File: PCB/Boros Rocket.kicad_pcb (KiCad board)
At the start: 6 copper layers, 100.6 x 100.6 mm, 44 parts, among them J1 B2B-XH-A, J2 TYPE-C-31-M-12, J3 Conn_01x02_Pin, Q1 MMBT3904, U1 BMP390, U2 IAM-20381, U3 ICM-42688-P, U4 MCP73831T-2DCI_MC, U5 RP2040, U6 USBLC6-2SC6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

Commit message: Refactor code structure for improved readability and maintainability
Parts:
- removed C10, C9: 100 nF, Capacitor_SMD:C_0603_1608Metric
- removed C11, C19: 1µF, Capacitor_SMD:C_0603_1608Metric
- removed C17, C18: 22pF, Capacitor_SMD:C_0603_1608Metric
- removed C20, C7, C8: 100nF, Capacitor_SMD:C_0603_1608Metric
- removed J3: Conn_01x02_Pin, Connector_PinHeader_2.54mm:PinHeader_1x02_P2.54mm_Vertical
- removed R5: 22Ω, Resistor_SMD:R_0603_1608Metric
- removed R7: 10k, Resistor_SMD:R_0603_1608Metric
- removed U5: RP2040, OPL:QFN40P700X700X90-57N
- removed U8: W25Q32JVSSIQ, OPL:SOIC127P790X216-8N
- removed Y1: 12MHz, Crystal:Crystal_SMD_3225-4Pin_3.2x2.5mm
- added J4: Conn_02x04_Counter_Clockwise, Connector_PinHeader_2.54mm:PinHeader_2x04_P2.54mm_Vertical, F.Cu at (136.8, 100.7)
- J2: value TYPE-C-31-M-12 -> 1981568-1; footprint OPL:HRO_TYPE-C-31-M-12 -> OPL:TE_1981568-1
- R1, R2: value 5.1 kΩ -> 100k
- R4: value 22Ω -> 10k
- U2: value IAM-20381 -> STM32G071K8TxN; footprint OPL:PQFN50P300X300X80-16N -> Package_QFP:LQFP-32_7x7mm_P0.8mm
- moved C5 83.1 mm to (154.4, 141.4), turned to 90 degrees
- moved J2 66.0 mm to (147.8, 148.3), turned to 0 degrees
- moved U1 63.9 mm to (130.1, 94.8), turned to 90 degrees
- moved U6 62.4 mm to (144.9, 137.7)
- moved R1 59.0 mm to (151.1, 137.6), turned to 0 degrees
- moved J1 59.0 mm to (194.4, 107.2), turned to -90 degrees
- moved R2 52.1 mm to (169.7, 71.6), turned to 0 degrees
- moved VR1 48.4 mm to (180.8, 109.7), turned to 0 degrees
- moved C12 47.6 mm to (120.9, 100.7), turned to 0 degrees
- moved C13 46.5 mm to (138.0, 90.0), turned to 0 degrees
- moved C15 46.2 mm to (183.2, 103.4), turned to 0 degrees
- moved U3 45.0 mm to (184.6, 83.0), turned to 90 degrees
- moved LS1 41.2 mm to (136.1, 60.2)
- moved C3 38.4 mm to (170.6, 110.2)
- moved C4 35.5 mm to (174.2, 100.5), turned to 90 degrees
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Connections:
- C5 pad 1: 3V3 -> GND
- C5 pad 2: GND -> USB_VBUS_SENSE
- C6 pad 1: 3V3 -> NRST
- R1 pad 1: GND -> USB_VBUS_SENSE
- R1 pad 2: Net-(J2-CC1) -> USB_VBUS
- R2 pad 1: GND -> USB_VBUS_SENSE
- R2 pad 2: Net-(J2-CC2) -> GND
- R4 pad 1: USB_DP -> 3V3
- R4 pad 2: Net-(U5-USB_DP) -> NRST
- U1 pad INT: BARO_INT -> unconnected-(U1-PadINT)
- U2 pad 1: 3V3 -> BUZZER_EN
- U2 pad 10: unconnected-(U2-RESV9_1215-Pad10)_1 -> UART_RX
- U2 pad 11: unconnected-(U2-RESV9_1215-Pad10) -> FLASH_CS
- U2 pad 12: unconnected-(U2-RESV9_1215-Pad10)_3 -> SPI_SCK
- U2 pad 13: GND -> SPI_MISO
- U2 pad 14: Net-(U2-REGOUT) -> SPI_MOSI
- U2 pad 15: unconnected-(U2-RESV9_1215-Pad10)_2 -> IMU_CS
- U2 pad 16: 3V3 -> BARO_CS
- U2 pad 2: SPI_SCK -> unconnected-(U2-PC14-Pad2)
- U2 pad 3: SPI_MOSI -> CHG_STAT
- U2 pad 4: SPI_MISO -> 3V3
- U2 pad 5: GYRO_CS -> GND
- U2 pad 6: IMU_INT -> NRST
- U2 pad 8: GND -> unconnected-(U2-PA1-Pad8)
- U2 pad 9: unconnected-(U2-RESV9_1215-Pad10)_4 -> UART_TX
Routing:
- net GND: track 0.00 -> 320.1 mm, vias 0 -> 6
- net 3V3: track 0.00 -> 178.8 mm, vias 0 -> 1
- net NRST: track 0.00 -> 100.9 mm, vias 0 -> 2
- net SPI_MOSI: track 0.00 -> 98.3 mm, vias 0 -> 4
- net VBAT: track 0.00 -> 97.9 mm, vias 0 -> 4
- net SPI_SCK: track 0.00 -> 87.2 mm, vias 0 -> 3
- net USB_VBUS_SENSE: track 0.00 -> 84.2 mm, vias 0 -> 2
- net SPI_MISO: track 0.00 -> 77.2 mm, vias 0 -> 2
- net USB_DM: track 0.00 -> 62.6 mm, vias 0 -> 3
- net CHG_STAT: track 0.00 -> 58.7 mm
- net USB_DP: track 0.00 -> 56.2 mm, vias 0 -> 2
- net USB_VBUS: track 0.00 -> 48.5 mm, vias 0 -> 2
- net BARO_CS: track 0.00 -> 46.6 mm, vias 0 -> 1
- net IMU_INT2: track 0.00 -> 46.3 mm, vias 0 -> 2
- net BUZZER_EN: track 0.00 -> 44.5 mm, vias 0 -> 2
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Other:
- copper layers 6 -> 4
- board text added: "+"
- board text added: "-"
- board text removed: "+ VBAT"
- board text removed: "- GND"

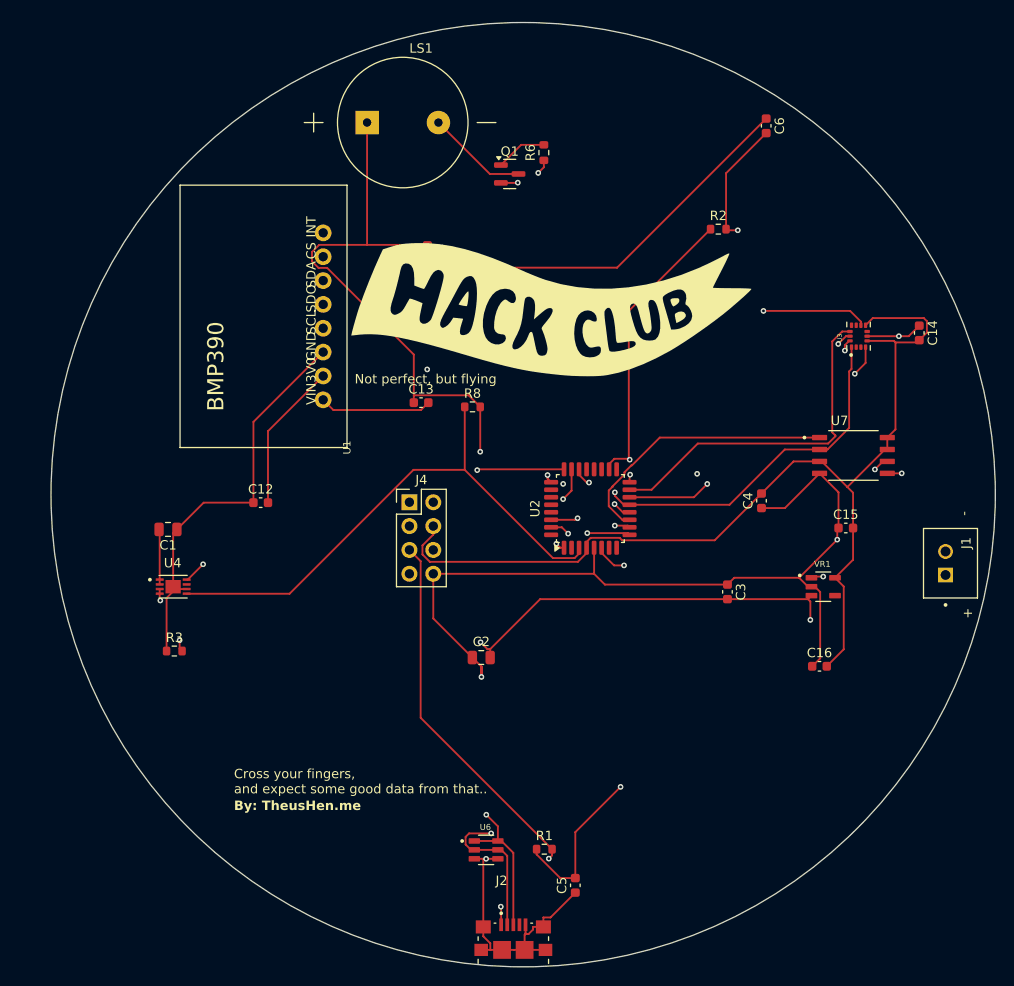
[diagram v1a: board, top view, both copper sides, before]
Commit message: Add Gerber job file for Boros Rocket PCB design
- Created a new Gerber job file 'Boros Rocket-job.gbrjob' for the Boros Rocket project.
- Included project specifications such as size, layer number, and board thickness.
- Defined design rules for outer and inner layers.
- Specified file attributes for copper layers, solder masks, silkscreens, and assembly drawings.
- Documented material stackup including thickness and type for each layer.
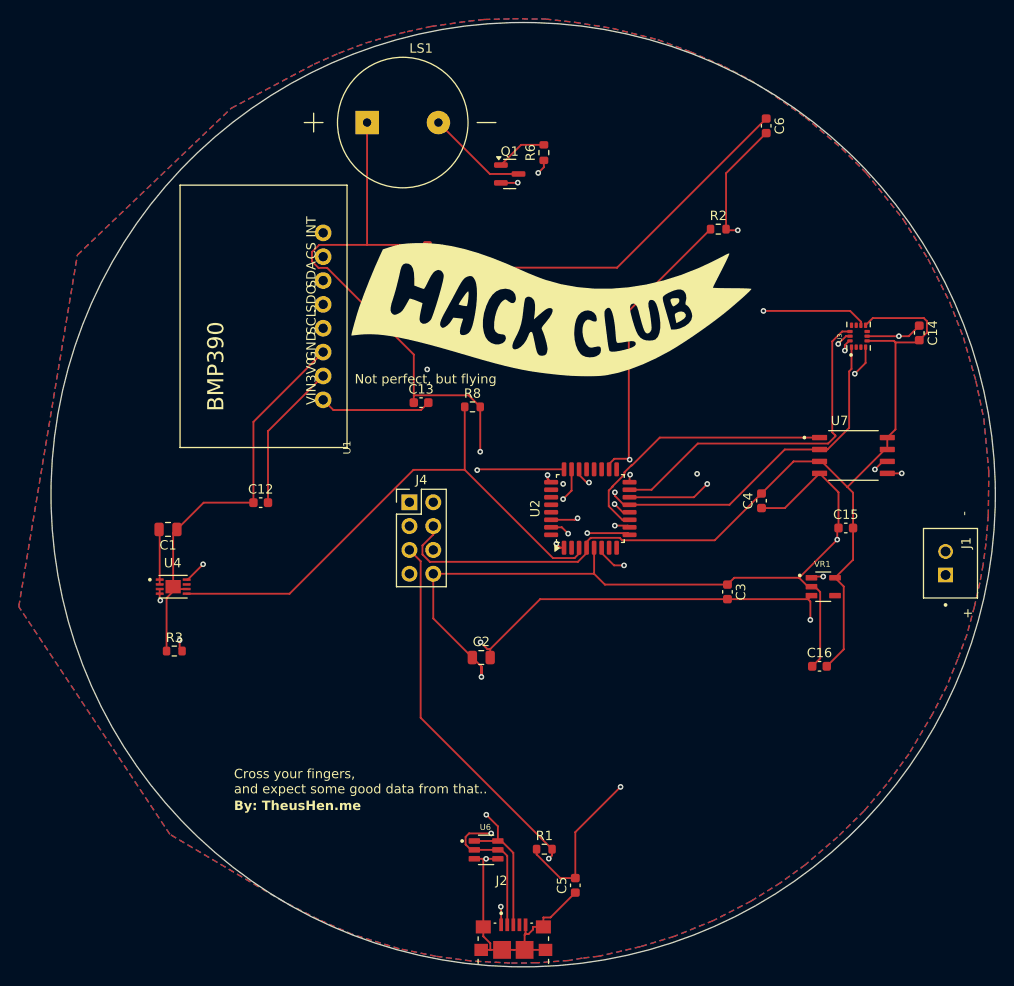
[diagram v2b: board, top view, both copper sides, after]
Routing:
- added copper zone on B.Cu, net GND
- added copper zone on F.Cu, net GND
- added copper zone on In1.Cu, net GND
- added copper zone on In2.Cu, net GND
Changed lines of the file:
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@@
 		(net 35)
+	)
+	(zone
+		(net 1)
+		(net_name "GND")
+		(layers "F.Cu" "B.Cu" "In1.Cu" "In2.Cu")
+		(hatch edge 0.5)
+		(connect_pads
+			(clearance 0.25)
+		)
+		(min_thickness 0.25)
+		(filled_areas_thickness no)
+		(fill yes
+			(thermal_gap 0.25)
+			(thermal_bridge_width 0.25)
+		)
+		(polygon
+			(pts
+				(xy 101.402549 74.33159) (xy 117.783536 58.701802) (xy 126.627221 54.000096) (xy 129.227221 52.850096)
+				(xy 132.127221 51.750096) (xy 134.702221 51.000096) (xy 136.502221 50.550096) (xy 139.027221 50.000096)
+				(xy 143.052221 49.425096) (xy 144.727221 49.250096) (xy 147.727221 49.175096) (xy 151.227221 49.200096)
+				(xy 154.377221 49.550096) (xy 158.402221 50.200096) (xy 163.202221 51.400096) (xy 166.702221 52.700096)
+				(xy 170.252221 54.250096) (xy 172.952221 55.650096) (xy 174.902221 56.850096) (xy 178.902221 59.650096)
+				(xy 182.802221 63.000096) (xy 185.427221 65.625096) (xy 189.352221 70.550096) (xy 191.977221 74.750096)
+				(xy 194.302221 79.375096) (xy 195.752221 83.125096) (xy 197.077221 87.725096) (xy 197.927221 91.775096)
+				(xy 198.452221 97.350096) (xy 198.402221 102.050096) (xy 198.152221 105.050096) (xy 197.852221 107.300096)
+				(xy 197.502221 109.225096) (xy 196.927221 111.750096) (xy 196.127221 114.750096) (xy 195.152221 117.350096)
+				(xy 194.002221 120.200096) (xy 192.477221 123.175096) (xy 189.952221 127.450096) (xy 187.602221 130.650096)
+				(xy 185.177221 133.525096) (xy 182.352221 136.300096) (xy 178.927221 139.250096) (xy 176.277221 141.175096)
+				(xy 173.152221 143.125096) (xy 169.127221 145.200096) (xy 164.977221 146.875096) (xy 161.377221 147.975096)
+				(xy 156.927221 149.000096) (xy 155.177221 149.200096) (xy 153.727221 149.450096) (xy 150.302221 149.700096)
+				(xy 147.477221 149.725096) (xy 143.302221 149.500096) (xy 139.577221 149.000096) (xy 135.677221 148.200096)
+				(xy 130.702221 146.675096) (xy 127.102221 145.100096) (xy 123.352221 143.175096) (xy 111.253797 136.016864)
+				(xy 95.162485 111.775178)
+			)
+		)
 	)
 	(embedded_fonts no)
